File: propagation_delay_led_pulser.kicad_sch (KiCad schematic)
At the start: 19 parts, among them J1 Conn_01x03, J2 Conn_01x02, J3 Conn_Coaxial, J4 Conn_Coaxial, J5 Conn_Coaxial, J6 Conn_01x02, U1 LTC1799, U2 74AC14, U3 74AHC1G00

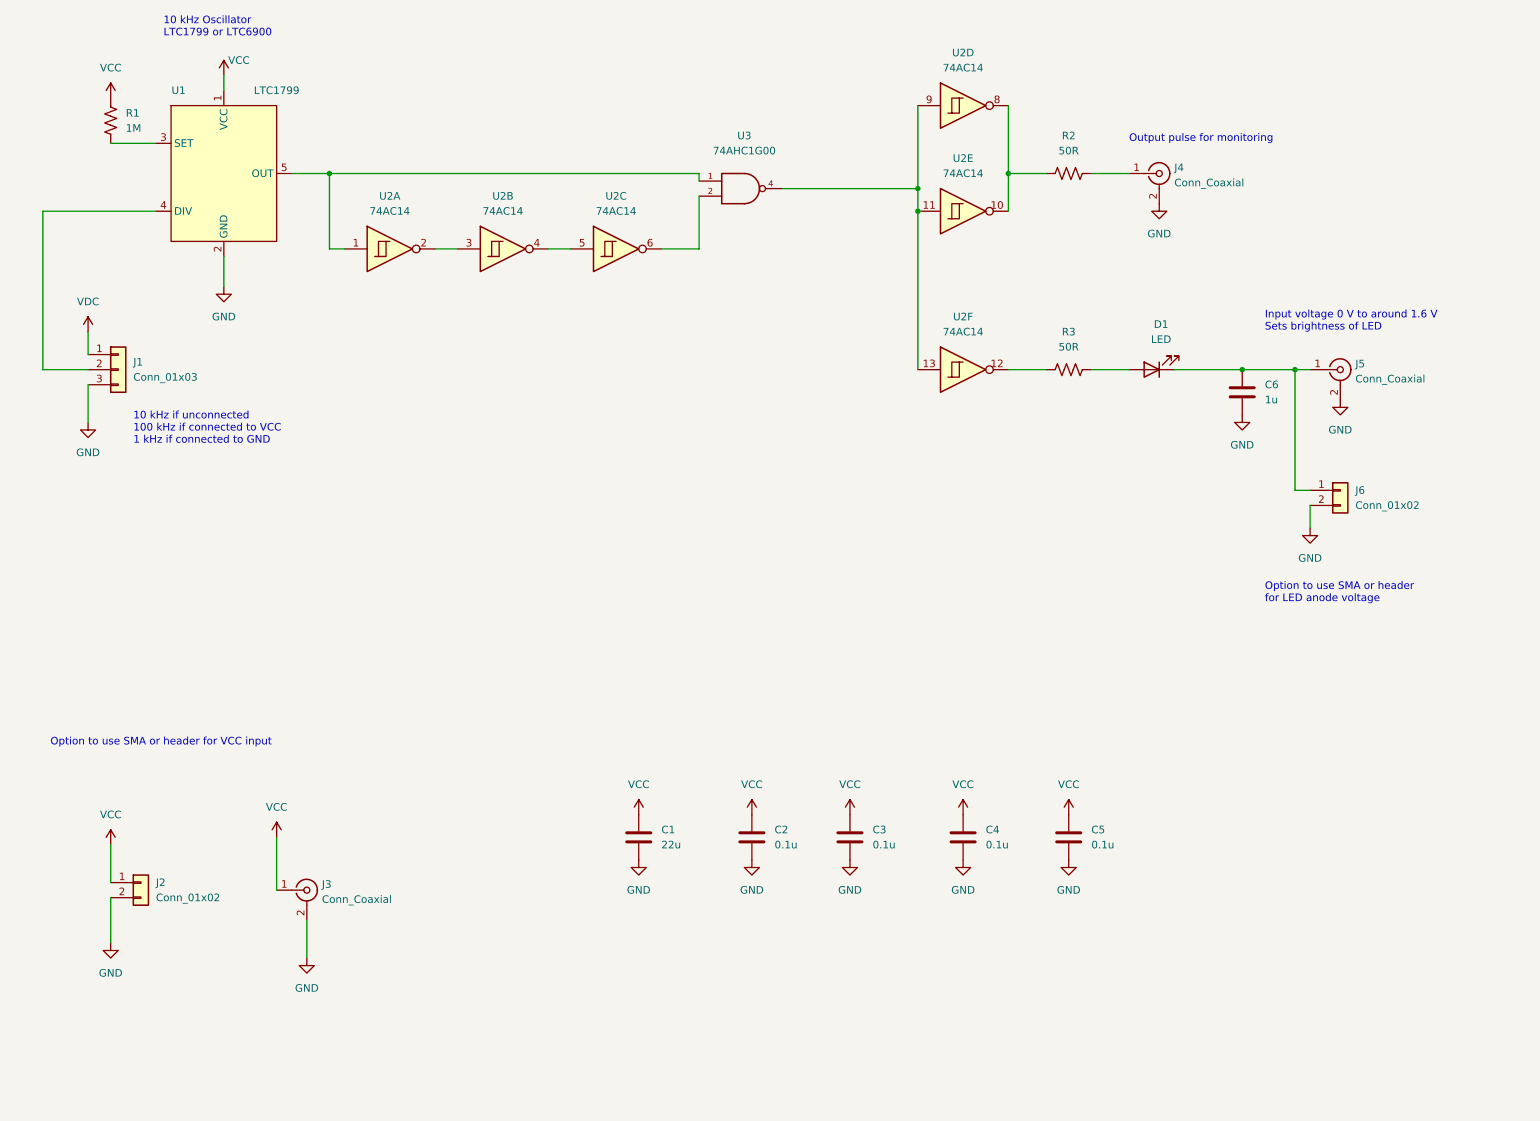
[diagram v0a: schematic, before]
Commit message: Switched to 555 for timer
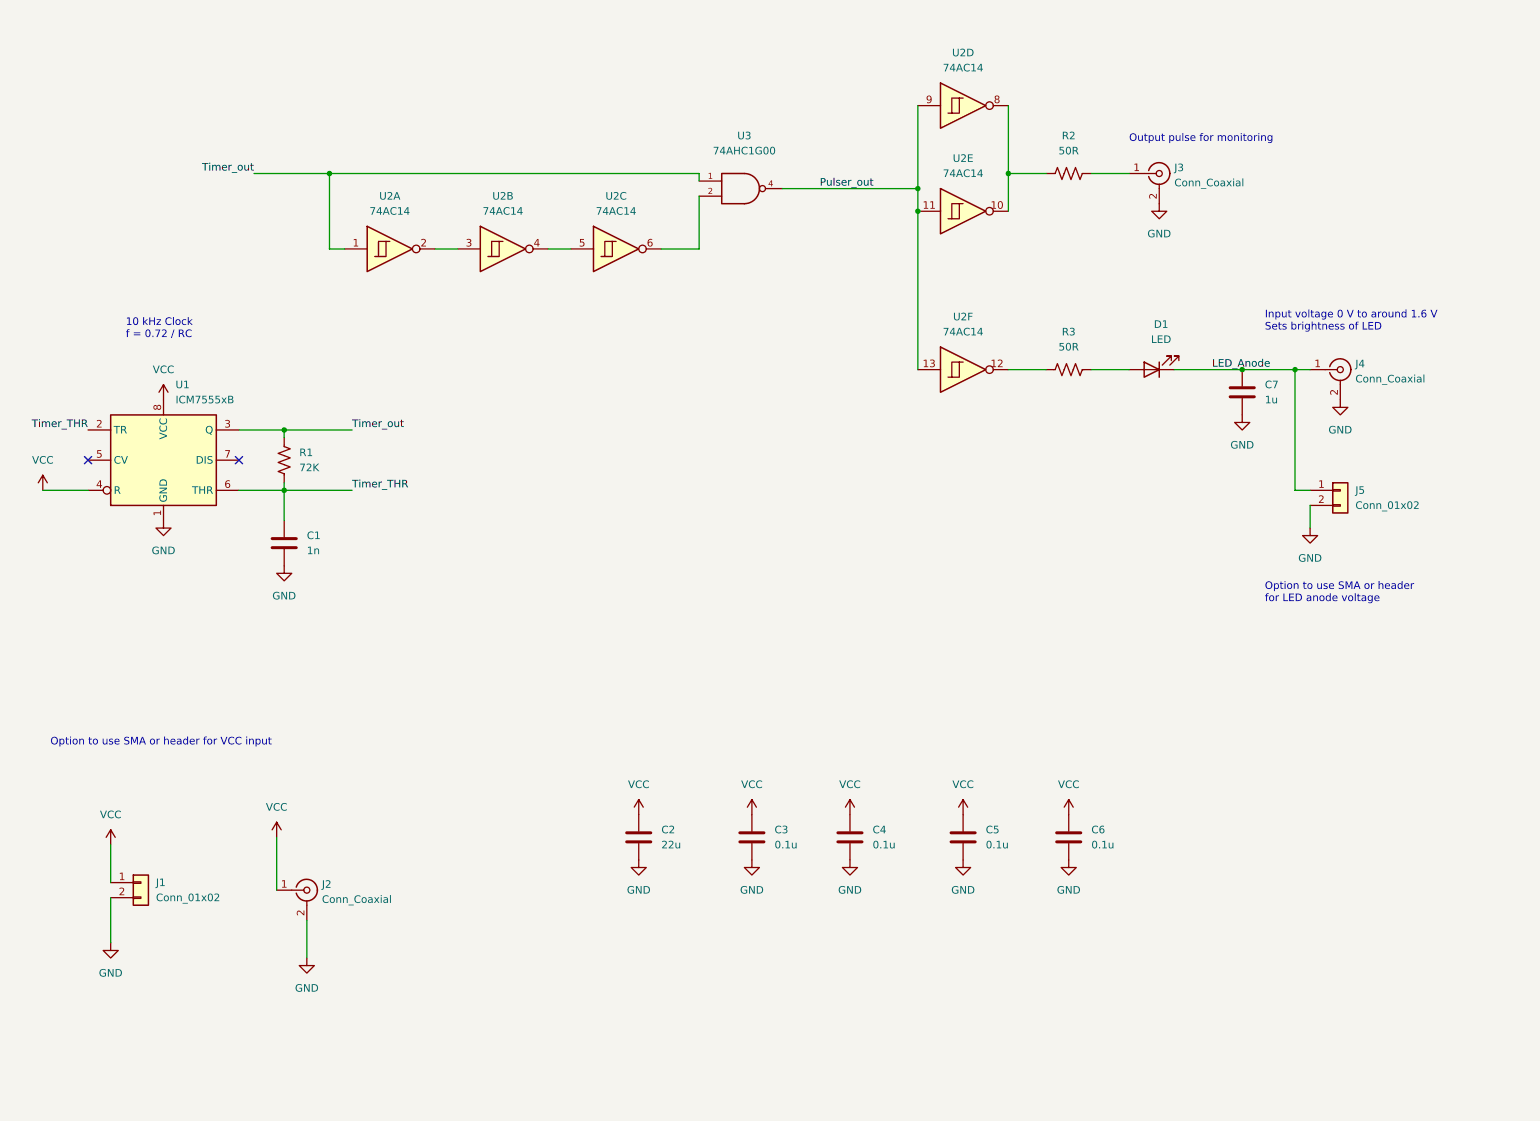
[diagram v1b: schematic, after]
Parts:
- removed J1: Conn_01x03, Connector_PinHeader_2.54mm:PinHeader_1x03_P2.54mm_Vertical, symbol Connector_Generic:Conn_01x03
- removed U1: LTC1799, Package_TO_SOT_SMD:SOT-23-5_HandSoldering, symbol my_library:LTC1799
- added C1: 1n, Capacitor_SMD:C_1206_3216Metric_Pad1.33x1.80mm_HandSolder, symbol Device:C
- added U1: ICM7555xB, Package_SO:SOIC-8_3.9x4.9mm_P1.27mm, symbol Timer:ICM7555xB
- R1: value 1M -> 72K; Part CRCW12061K00FKEAC -> CRCW120671K5FKEA
- renumbered C1 to C2, C2 to C3, C3 to C4, C4 to C5, C5 to C6, C6 to C7, J2 to J1, J3 to J2, J4 to J3, J5 to J4, J6 to J5
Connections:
- net GND: now also C1.2, U1.1 (GND)
- net VCC: now also U1.4 (R), U1.8 (VCC); no longer R1.1
- net Pulser_out: now reaches U2.11, U2.13, U2.9, U3.4
- net LED_Anode: now reaches C7.1, D1.1 (K), J4.1 (In), J5.1 (Pin_1)
- net Timer_out: now reaches U2.1, U3.1
- net Timer_out: now also R1.1, U1.3 (Q)
- net Timer_THR: now reaches R1.2
- net Timer_THR: now also C1.1, U1.2 (TR), U1.6 (THR)
- no-connect marks 0 -> 2
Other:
- note added: "10 kHz Clock f = 0.72 / RC"
- note removed: "10 kHz Oscillator LTC1799 or LTC6900"
- note removed: "10 kHz if unconnected 100 kHz if connected to VCC 1 kHz if connected to GND"

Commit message: Changed headers to one nano-fit
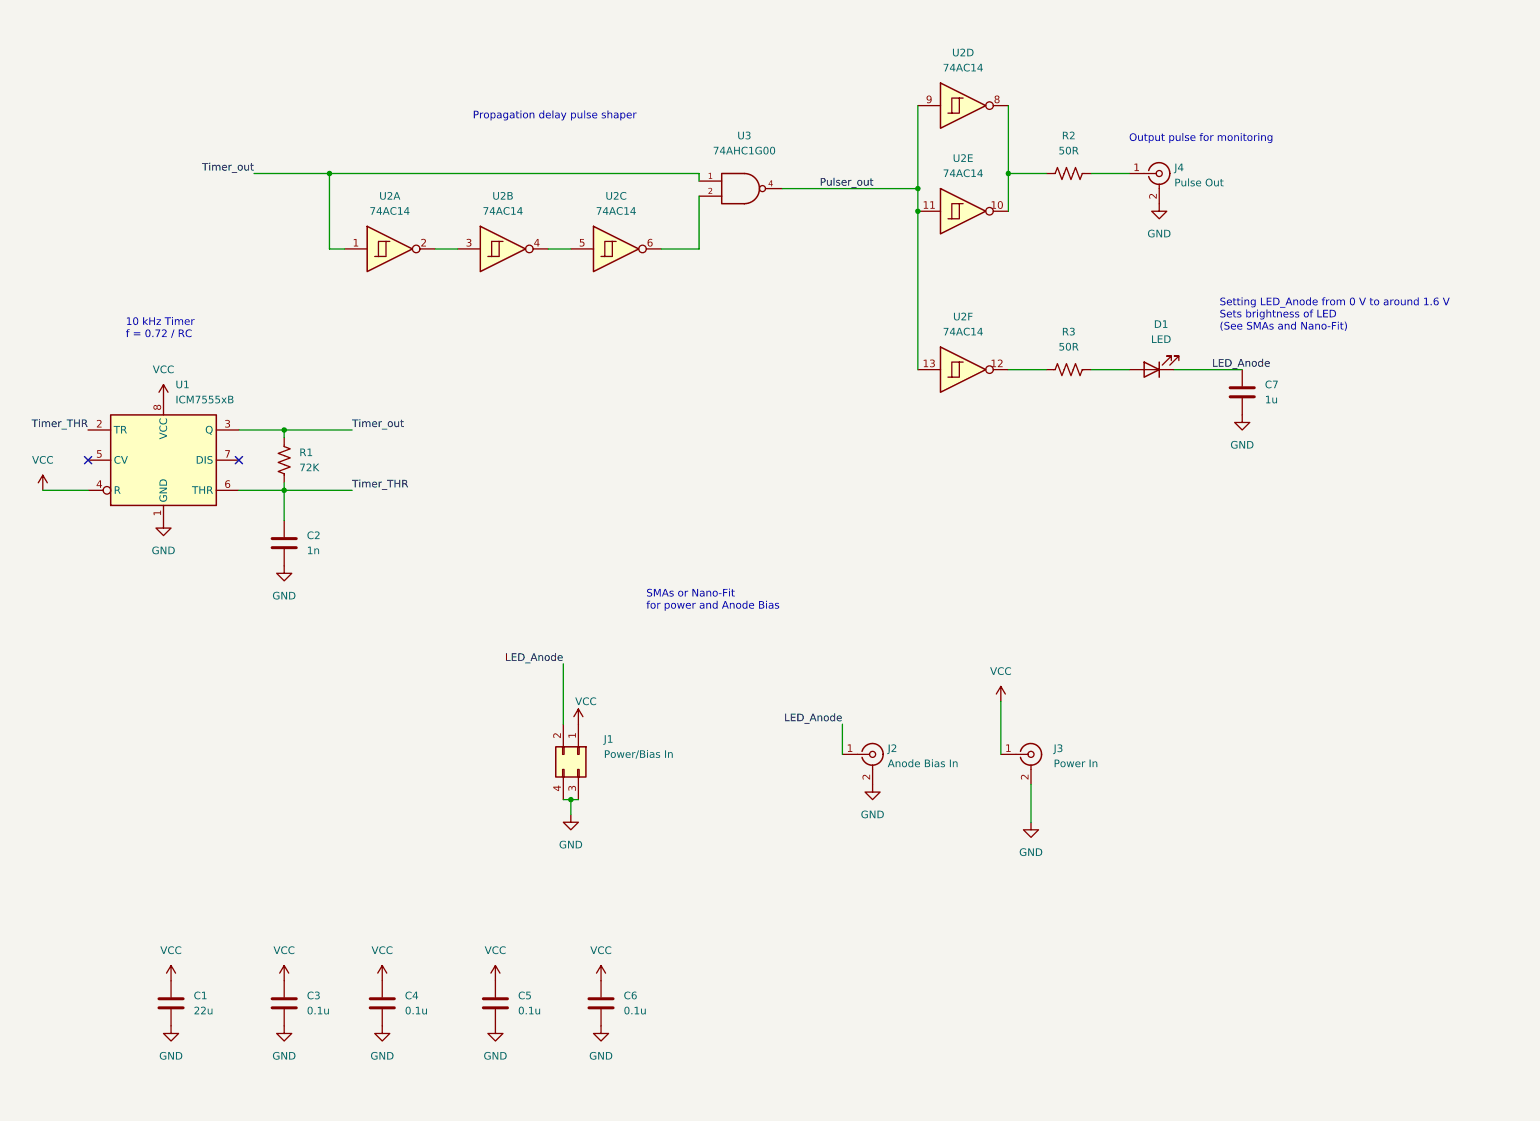
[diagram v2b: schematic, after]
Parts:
- removed J1, J5: Conn_01x02, Connector_PinHeader_2.54mm:PinHeader_1x02_P2.54mm_Vertical, symbol Connector_Generic:Conn_01x02
- removed J4: Conn_Coaxial, Connector_Coaxial:SMA_Amphenol_132289_EdgeMount, symbol Connector:Conn_Coaxial
- added J1: Power/Bias In, Connector_Molex:Molex_Nano-Fit_105314-xx04_2x02_P2.50mm_Horizontal, symbol Connector_Generic:Conn_02x02_Top_Bottom
- added J2: Anode Bias In, Connector_Coaxial:SMA_Amphenol_132289_EdgeMount, symbol Connector:Conn_Coaxial
- J3: renamed from J2; value Conn_Coaxial -> Power In
- J4: renamed from J3; value Conn_Coaxial -> Pulse Out
- renumbered C2 to C1, C1 to C2
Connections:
- net GND: now also J1.3 (Pin_3), J1.4 (Pin_4), J2.2 (Ext)
- net LED_Anode: now also J1.2 (Pin_2), J2.1 (In)
- net VCC: now also J1.1 (Pin_1)
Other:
- note added: "10 kHz Timer f = 0.72 / RC"
- note added: "Propagation delay pulse shaper"
- note added: "SMAs or Nano-Fit for power and Anode Bias"
- note added: "Setting LED_Anode from 0 V to around 1.6 V Sets brightness of LED (See SMAs and Nano-Fit)"
- note removed: "10 kHz Clock f = 0.72 / RC"
- note removed: "Input voltage 0 V to around 1.6 V Sets brightness of LED"
- note removed: "Option to use SMA or header for LED anode voltage"
- note removed: "Option to use SMA or header for VCC input"
- moved on the sheet: C1, C3, C4, C5, C6, J3

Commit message: removed pwr/bias SMAs and initial PCB placement
  also added mfr/part for timer capacitor
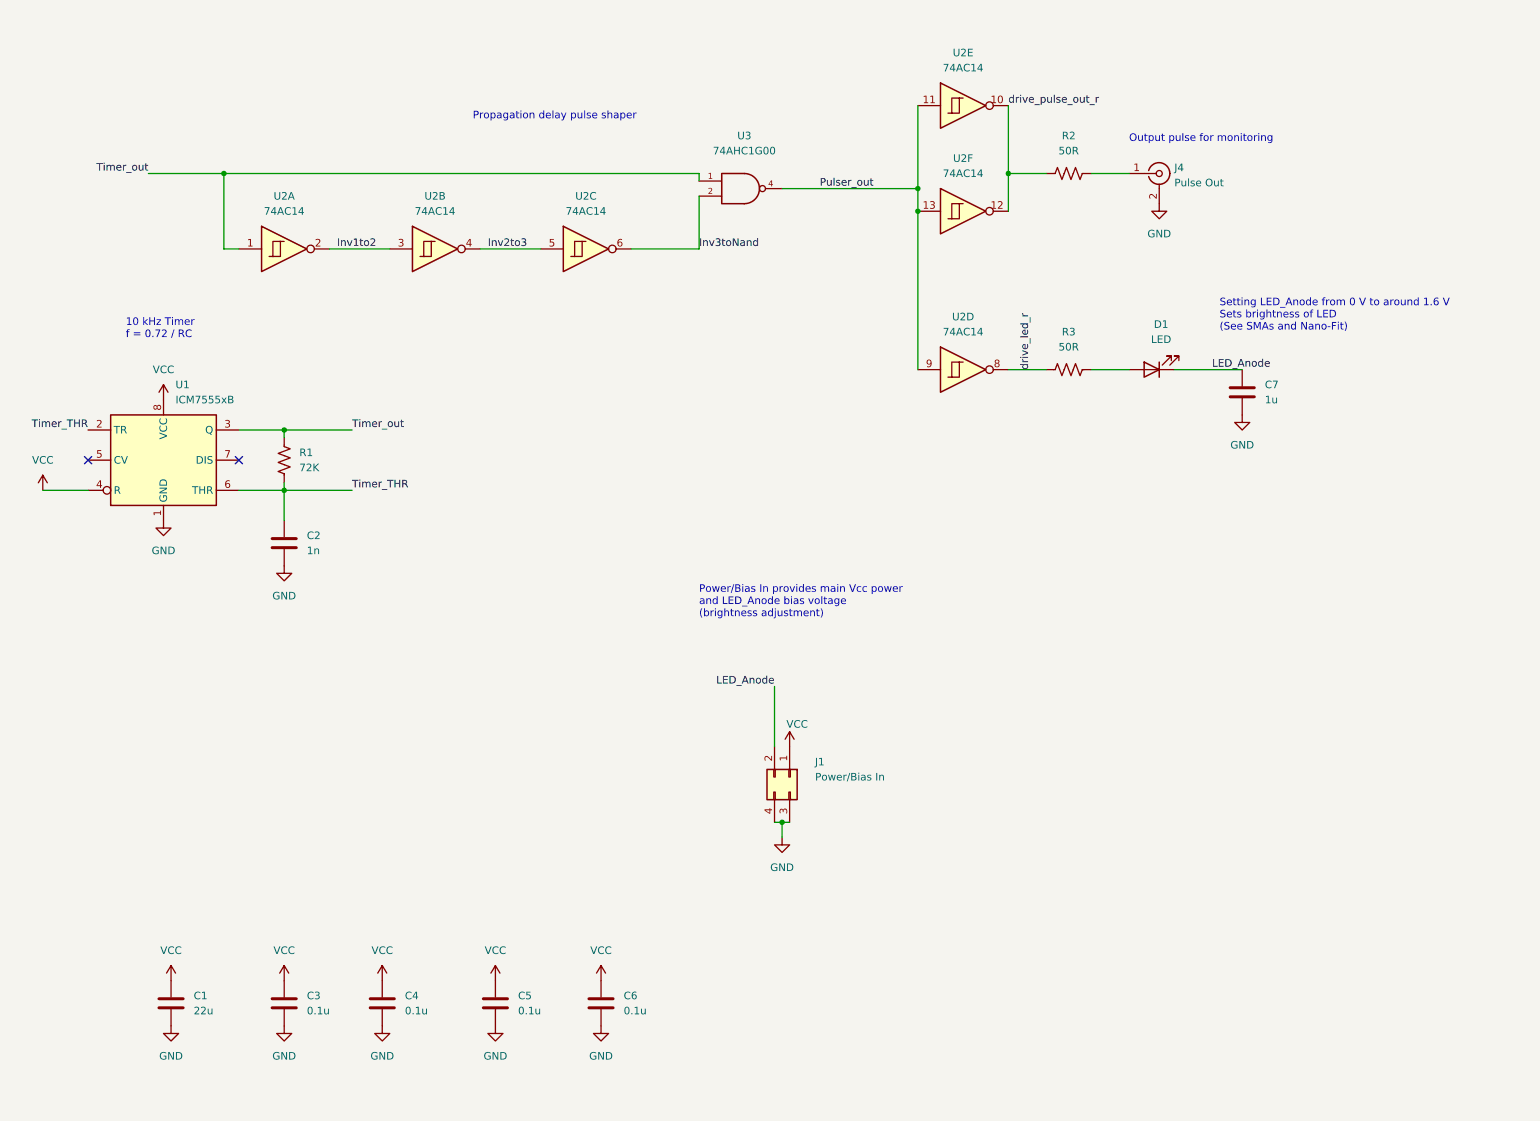
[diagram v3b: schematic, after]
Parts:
- removed J2: Anode Bias In, Connector_Coaxial:SMA_Amphenol_132289_EdgeMount, symbol Connector:Conn_Coaxial
- removed J3: Power In, Connector_Coaxial:SMA_Amphenol_132289_EdgeMount, symbol Connector:Conn_Coaxial
- C2: Mfr (none) -> Kyocera AVX; Part (none) -> 12063A102FAT2A
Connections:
- net Pulser_out: now also U2.11, U2.13, U2.9; no longer U2.11, U2.13, U2.9
- net Inv1to2: now reaches U2.2, U2.3
- net drive_led_r: now reaches R3.1
- net drive_led_r: now also U2.8; no longer U2.12
- net Inv2to3: now reaches U2.4, U2.5
- net Inv3toNand: now reaches U2.6, U3.2
- new net drive_pulse_out_r: R2.1, U2.10, U2.12
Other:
- note added: "Power/Bias In provides main Vcc power and LED_Anode bias voltage (brightness adjustment)"
- note removed: "SMAs or Nano-Fit for power and Anode Bias"
- moved on the sheet: J1, U2A, U2B, U2C

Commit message: Added board outline
  aligned connectors with outline
  added power for inverter to schematic
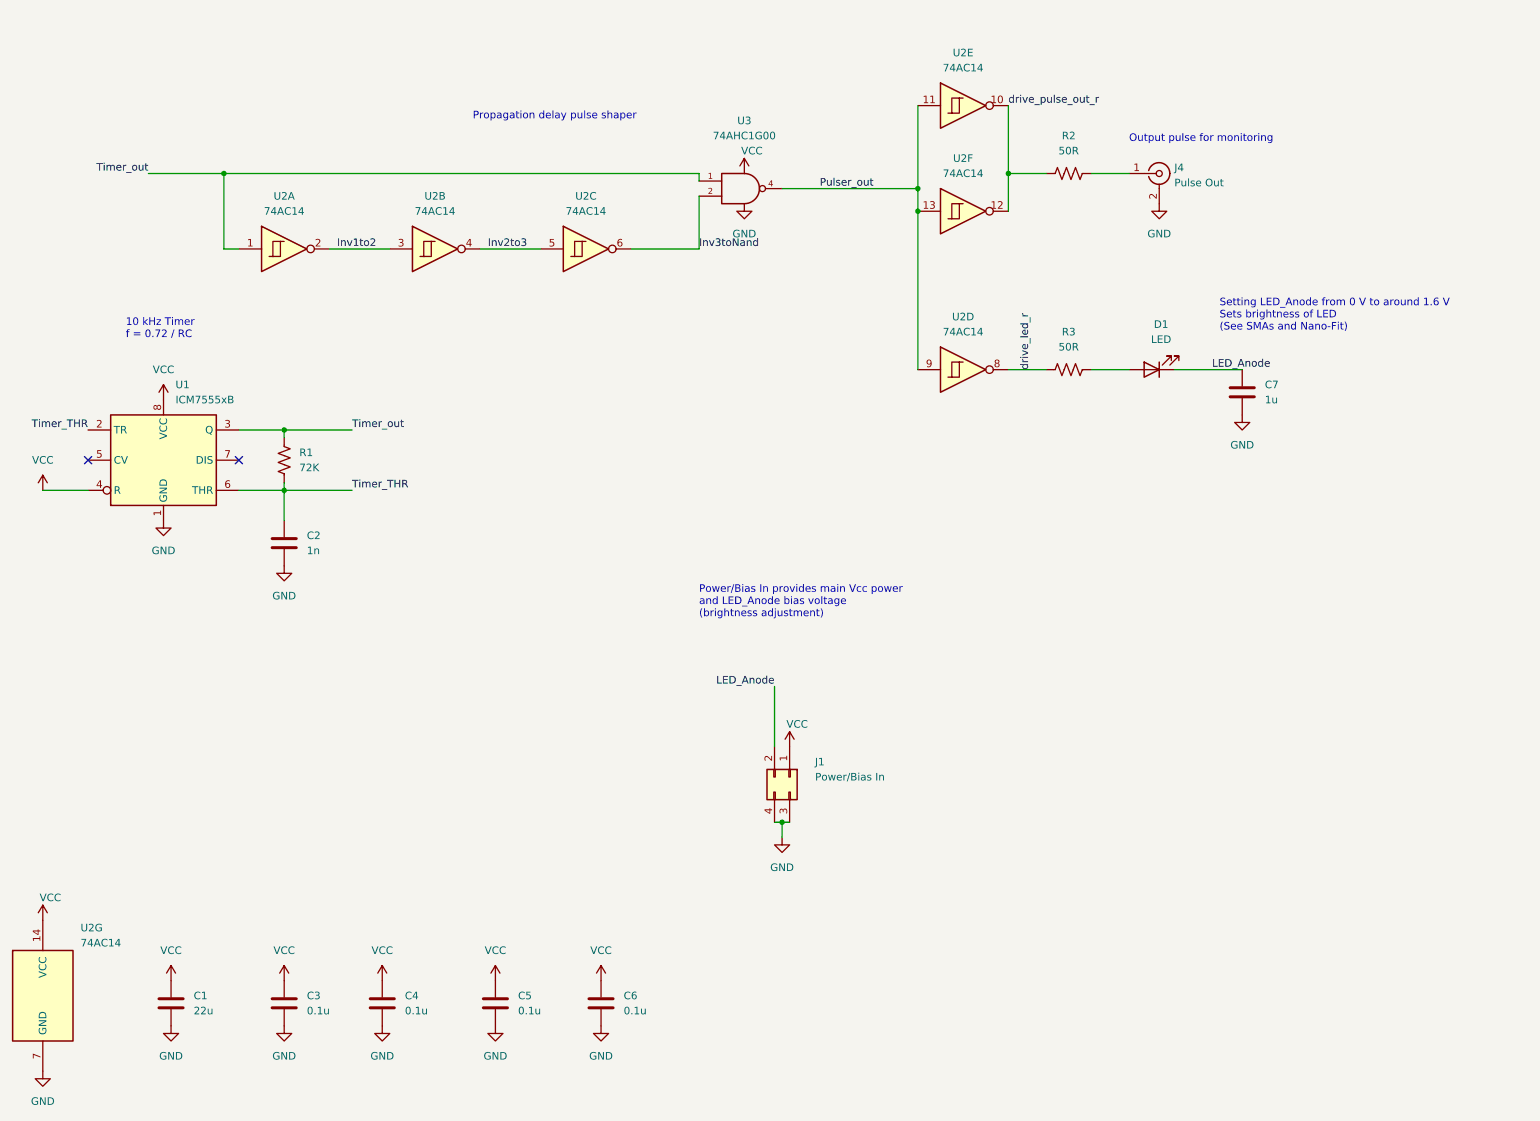
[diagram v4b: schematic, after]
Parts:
- added unit 7 of U2
- U2: footprint Package_SO:SOIC-14_3.9x8.7mm_P1.27mm -> (none)
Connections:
- net GND: now also U2.7 (GND)
- net VCC: now also U2.14 (VCC)
